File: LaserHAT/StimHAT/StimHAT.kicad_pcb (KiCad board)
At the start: 4 copper layers, 65 x 57 mm, 112 parts, among them J1 GPIO, J10 OLED 0.91 (GND VCC SCL SDA), J101 ELECTRODE E1/E2, J102 B4B-PH-K-S(LF)(SN), J103 5V TO DC-DC POD, J5 GT-USB-7010ASV, J6 BNC TRIGGER IN, J7 BNC STIM OUT, Q3 AP30P30Q, Q4 DMMT5401, Q5 AP30P30Q, SW10 MSK12C02, SW6 TS-1088-AR02016, SW7 SKRHADE010, SW9 TS-1088-AR02016, U1 M24C32-WDW6TP, U101 ISO7741FDBQR, U104 TLV76050DBZR, U105 DAC60501ZDGSR, U106 OPA2192IDGKR, U107 CD74HC4053PWR, U108 DG418DY-T1-E3, U109 ISO1640BDR, U110 TLV1702AIDGKR, U4 MCP1700T-3302E/MB, U5 AP2171W, U6 CH340N, U7 MSPM0G1507SRHBR, U8 74LVC2G17GW

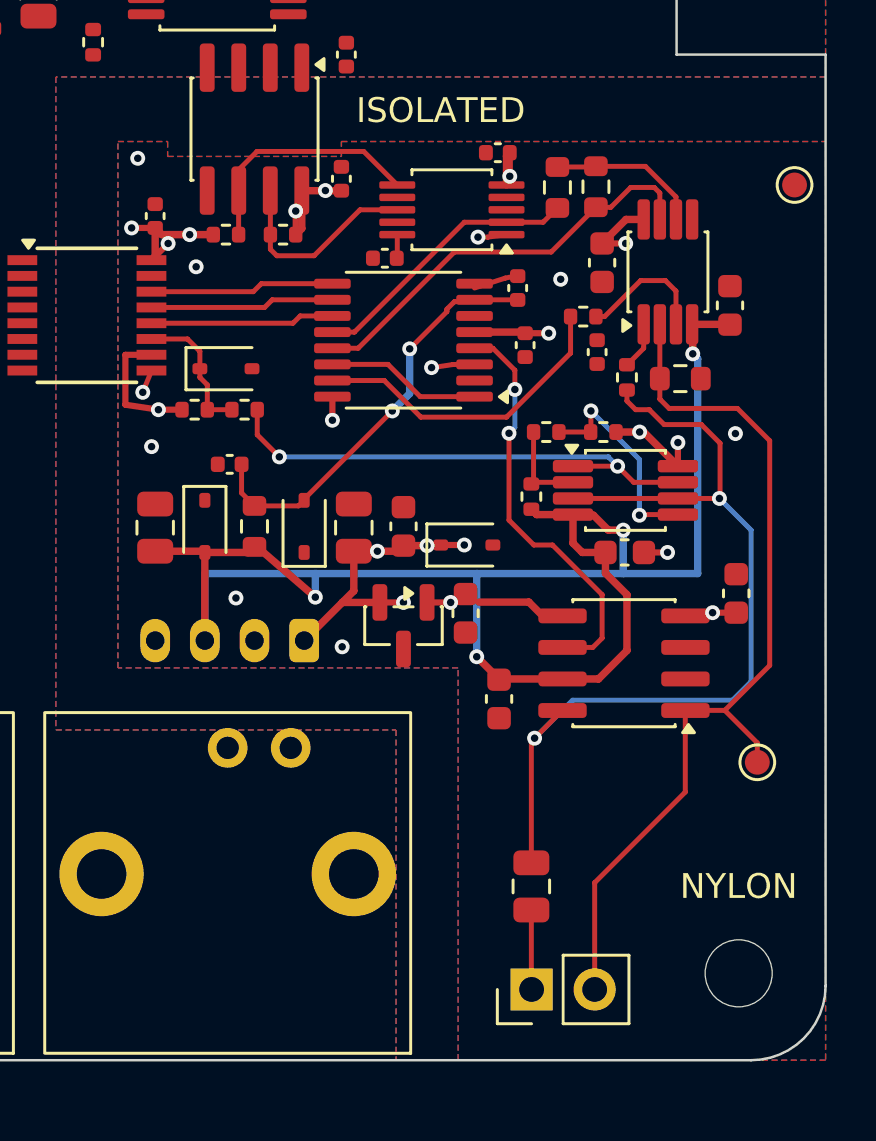
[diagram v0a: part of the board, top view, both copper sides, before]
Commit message: Cleaned up routing
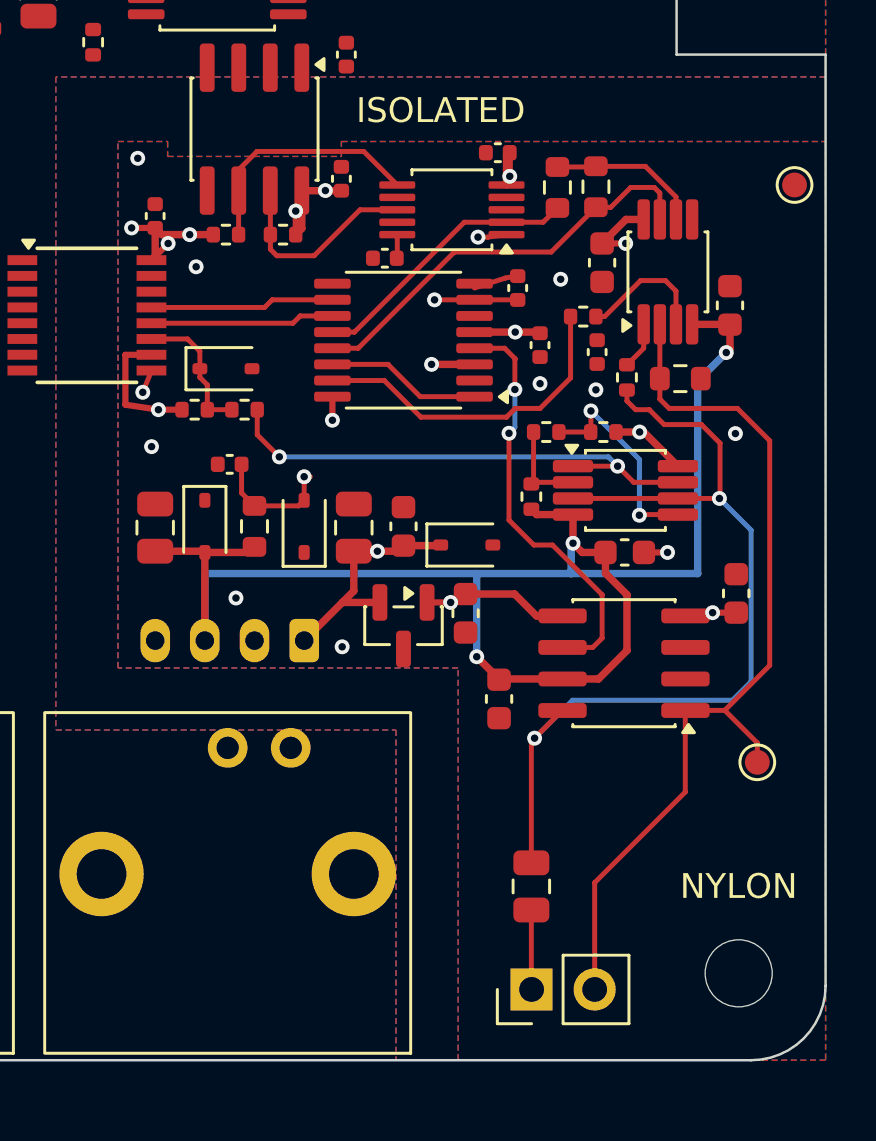
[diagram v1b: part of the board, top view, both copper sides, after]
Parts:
- moved C118 0.60 mm to (53.5, 28.2)
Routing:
- net +V_STIM: track 65.6 -> 54.1 mm, vias 9 -> 5
- net RELEASE: track 7.42 -> 0.00 mm
- net -V_STIM: track 69.1 -> 62.1 mm, vias 4 -> 3
- net +5V_ISO: track 87.7 -> 81.7 mm
- net -5V_ISO: track 17.1 -> 18.7 mm
- net SCL: track 9.87 -> 9.02 mm
- net V_IN: track 12.7 -> 13.3 mm
- net GND_ISO: track 4.48 -> 4.53 mm, vias 9 -> 11
